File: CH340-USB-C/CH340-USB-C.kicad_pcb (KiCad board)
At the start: 2 copper layers, 18 parts, among them J1 USB_C_Receptacle_USB2.0, J2 Conn_01x05_Female, SW1 SW_Push_SPDT, U1 XC6206PxxxMR, U2 CH340N

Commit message: 初步排好電路板
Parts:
- moved J2 51.9 mm to (144.3, 105.6), turned to 180 degrees
- moved F1 42.4 mm to (74.2, 104.4), turned to -90 degrees
- moved J1 35.2 mm to (67.5, 96.5), turned to -90 degrees
- moved C1 35.2 mm to (76.5, 104.4), turned to -90 degrees
- moved C3 29.6 mm to (82.5, 99.5), turned to 90 degrees
- moved C4 25.6 mm to (82.5, 96.0), turned to -90 degrees
- moved U2 24.0 mm to (77.6, 98.0)
- moved SW1 19.8 mm to (77.8, 88.9), turned to 180 degrees
- moved C2 16.4 mm to (82.0, 104.4), turned to 90 degrees
- moved U1 14.2 mm to (79.3, 104.5), turned to 90 degrees

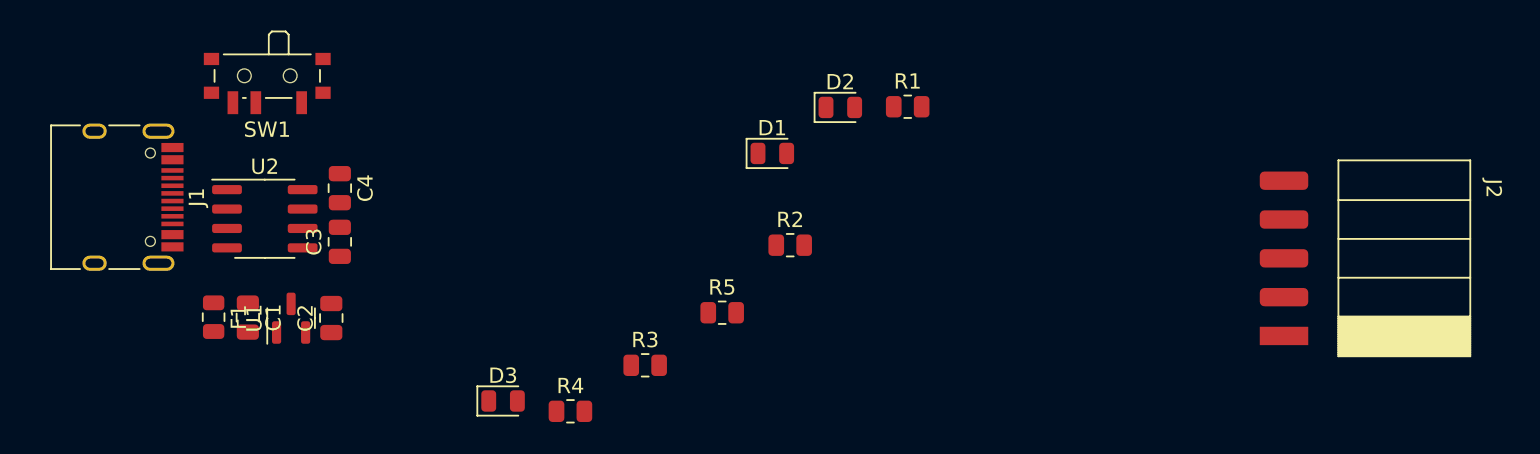
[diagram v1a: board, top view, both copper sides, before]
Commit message: 放置零件及佈線
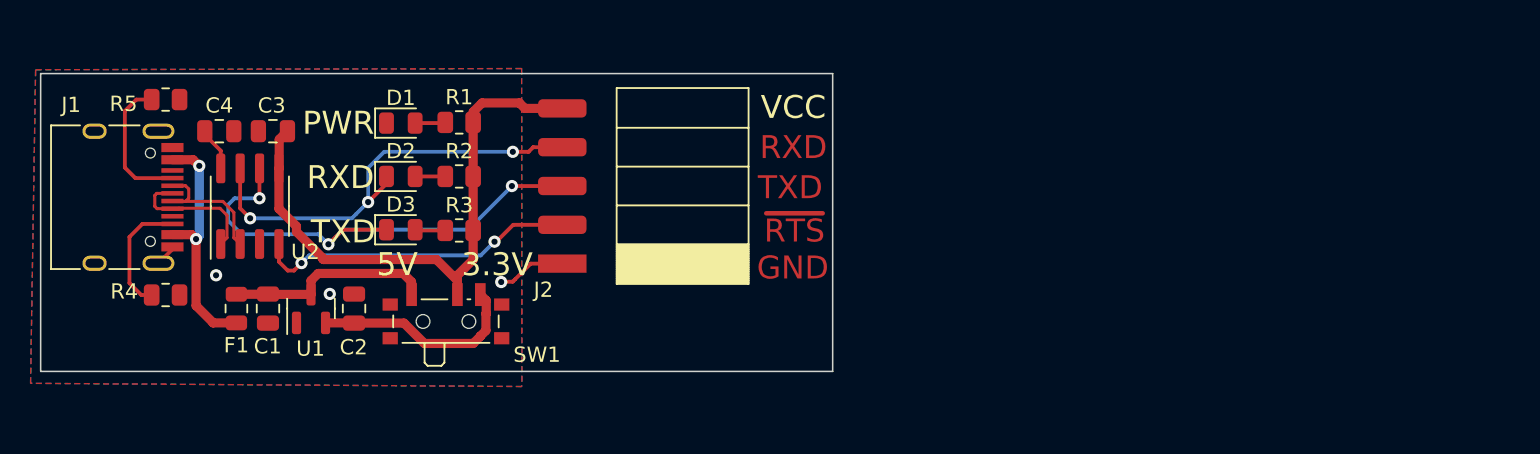
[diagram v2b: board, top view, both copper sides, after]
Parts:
- moved J2 47.5 mm to (97.1, 100.9)
- moved R5 39.0 mm to (71.1, 90.2), turned to 180 degrees
- moved R1 29.4 mm to (90.3, 91.6)
- moved D2 29.1 mm to (86.5, 95.2)
- moved R4 27.6 mm to (71.1, 102.9), turned to 180 degrees
- moved D1 24.4 mm to (86.5, 91.7)
- moved R2 22.1 mm to (90.3, 95.2)
- moved SW1 19.4 mm to (89.5, 104.3), turned to 0 degrees
- moved R3 15.0 mm to (90.3, 98.7)
- moved D3 13.1 mm to (86.5, 98.7)
- moved C4 8.73 mm to (74.6, 92.2), turned to 0 degrees
- moved C3 8.46 mm to (78.1, 92.2), turned to 180 degrees
- moved C2 1.61 mm to (83.4, 103.8)
- moved F1 1.59 mm to (75.7, 103.8), turned to 90 degrees
- moved U1 1.45 mm to (80.6, 103.8)
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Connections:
- R1 pad 2: +5V -> VCC
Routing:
- net VCC: track 0.00 -> 37.8 mm
- net /TXD: track 0.00 -> 33.5 mm, vias 0 -> 3
- net /RXD: track 0.00 -> 29.4 mm, vias 0 -> 3
- net /~{RTS}: track 0.00 -> 21.2 mm, vias 0 -> 2
- net Net-(F1-Pad1): track 0.00 -> 15.9 mm, vias 0 -> 2
- net +3V3: track 0.00 -> 13.9 mm
- net +5V: track 0.00 -> 13.6 mm
- net /CC1: track 0.00 -> 9.17 mm
- net /USBD+: track 0.00 -> 8.97 mm
- net /USBD-: track 0.00 -> 8.62 mm
- net /CC2: track 0.00 -> 7.97 mm
- net GND: track 0.00 -> 5.94 mm, vias 0 -> 3
- net /3V3: track 0.00 -> 2.87 mm
- net Net-(D3-Pad2): track 0.00 -> 1.99 mm
- net Net-(D1-Pad2): track 0.00 -> 1.99 mm
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- added copper zone on B.Cu, net GND
- added copper zone on F.Cu, net GND
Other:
- board outline added: 51.8 x 19.5 mm
- board text added: "3.3V"
- board text added: "5V"
- board text added: "GND"
- board text added: "PWR"
- board text added: "RXD"
- board text added: "TXD"
- board text added: "VCC"
- board text added: "~{RTS}"

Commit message: 調整布局
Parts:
- J2: moved to B.Cu
- moved J2 18.0 mm to (82.3, 90.6)
- moved R5 14.8 mm to (71.1, 104.9)
- moved R3 3.60 mm to (90.3, 95.1)
- moved D3 3.54 mm to (86.5, 95.1)
- moved D2 3.40 mm to (86.5, 98.6)
- moved R2 3.40 mm to (90.3, 98.6)
- moved SW1 2.31 mm to (91.8, 104.4)
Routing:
- net /TXD: track 33.5 -> 12.4 mm, vias 3 -> 2
- net /RXD: track 29.4 -> 13.9 mm, vias 3 -> 2
- net +3V3: track 13.9 -> 23.6 mm, vias 0 -> 2
- net GND: track 5.94 -> 1.45 mm, vias 3 -> 12
- net /CC1: track 9.17 -> 13.2 mm
- net +5V: track 13.6 -> 16.3 mm
- net /~{RTS}: track 21.2 -> 18.7 mm, vias 2 -> 1
- net VCC: track 37.8 -> 38.5 mm, vias 0 -> 1
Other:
- board size 51.8 x 19.5 mm -> 37.2 x 19.5 mm

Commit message: 調整布局
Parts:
- added TP1: TestPoint, TestPoint:TestPoint_Pad_D2.0mm, F.Cu at (97.9, 94.6)
- added TP2: TestPoint, TestPoint:TestPoint_Pad_D2.0mm, F.Cu at (97.9, 98.4)
- added TP3: TestPoint, TestPoint:TestPoint_Pad_D2.0mm, F.Cu at (94.2, 90.8)
- added TP4: TestPoint, TestPoint:TestPoint_Pad_D2.0mm, F.Cu at (97.9, 90.8)
- added TP5: TestPoint, TestPoint:TestPoint_Pad_D2.0mm, F.Cu at (94.1, 98.4)
- added TP6: TestPoint, TestPoint:TestPoint_Pad_D2.0mm, F.Cu at (94.2, 94.7)
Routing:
- net +5V: track 16.3 -> 35.3 mm
- net /RXD: track 13.9 -> 25.7 mm, vias 2 -> 3
- net /TXD: track 12.4 -> 24.0 mm, vias 2 -> 3
- net +3V3: track 23.6 -> 31.9 mm
- net VCC: track 38.5 -> 41.5 mm
- net GND: vias 12 -> 9

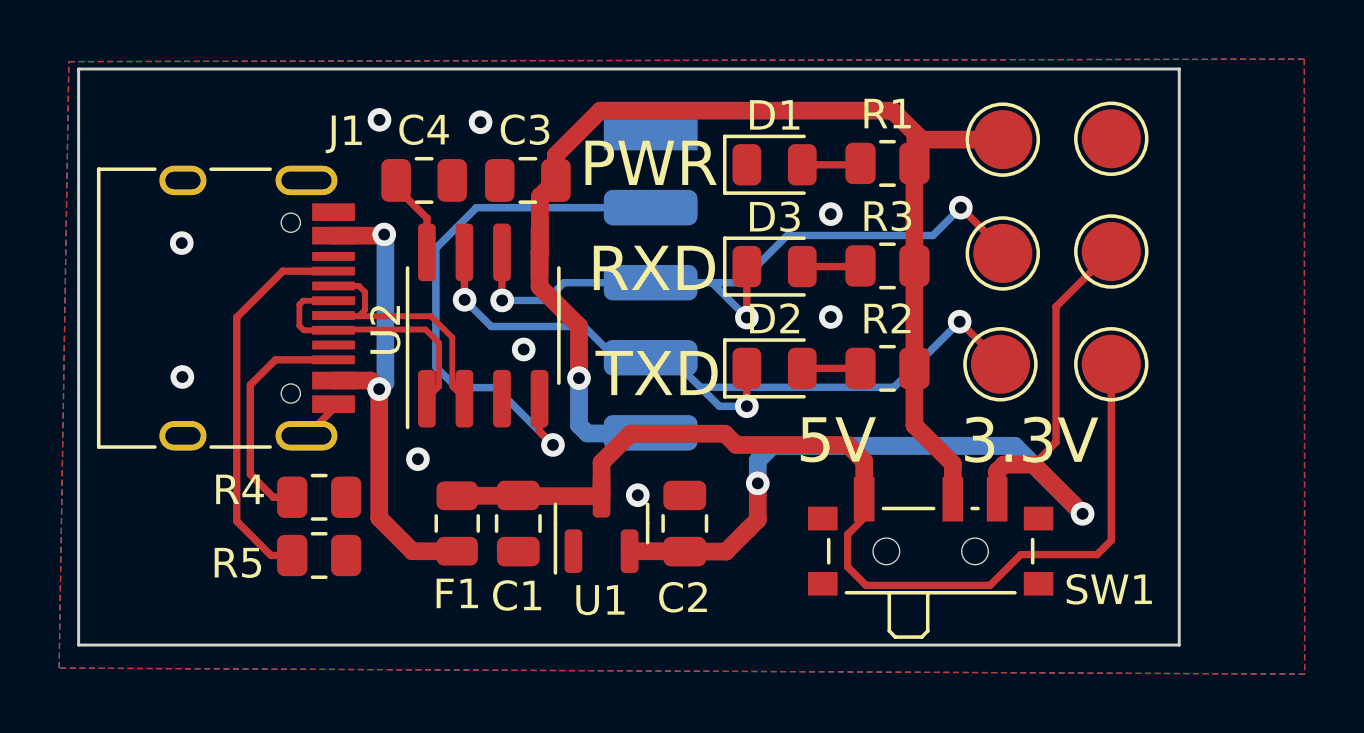
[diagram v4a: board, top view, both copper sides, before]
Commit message: 重新鋪銅
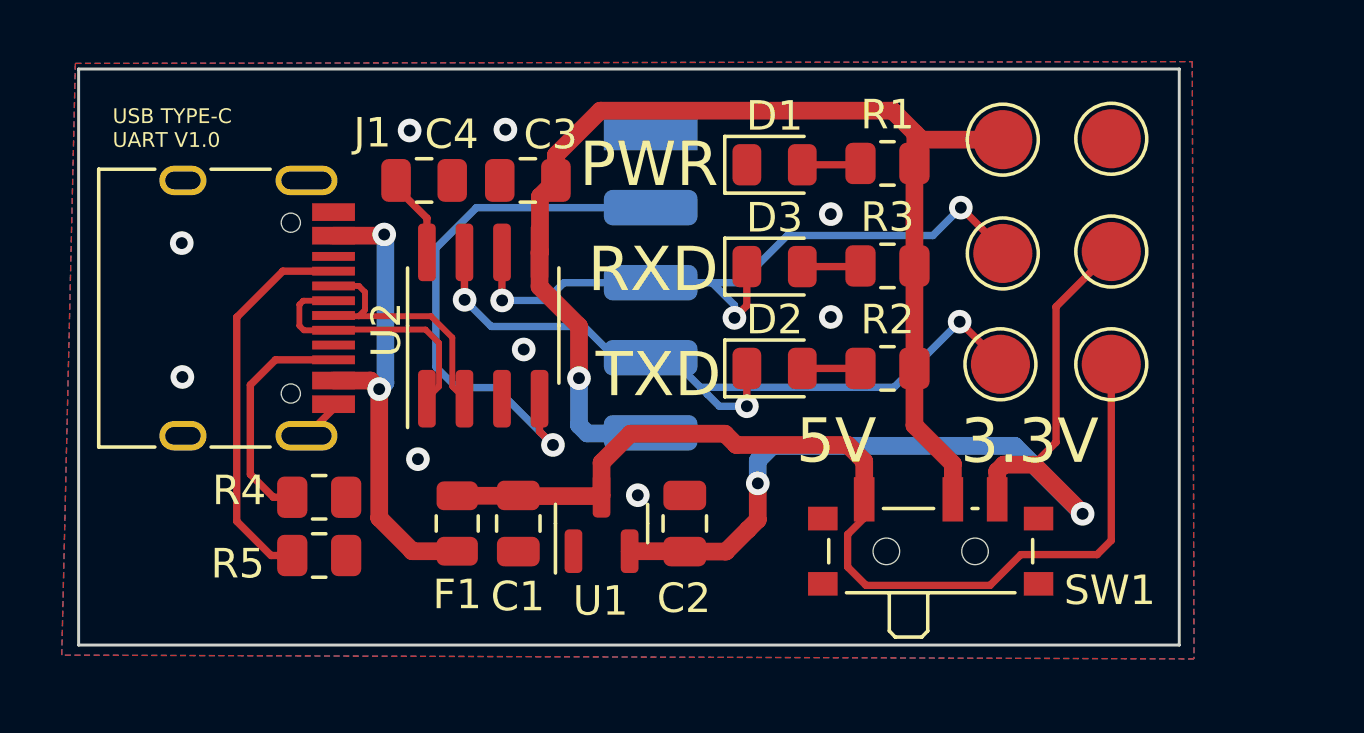
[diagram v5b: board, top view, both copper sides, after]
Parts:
- added REF**: KiCad-Logo2_5mm_SilkScreen, Symbol:KiCad-Logo2_5mm_SilkScreen, B.Cu at (72.1, 104.2)
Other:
- board text added: "USB TYPE-C UART V1.0"

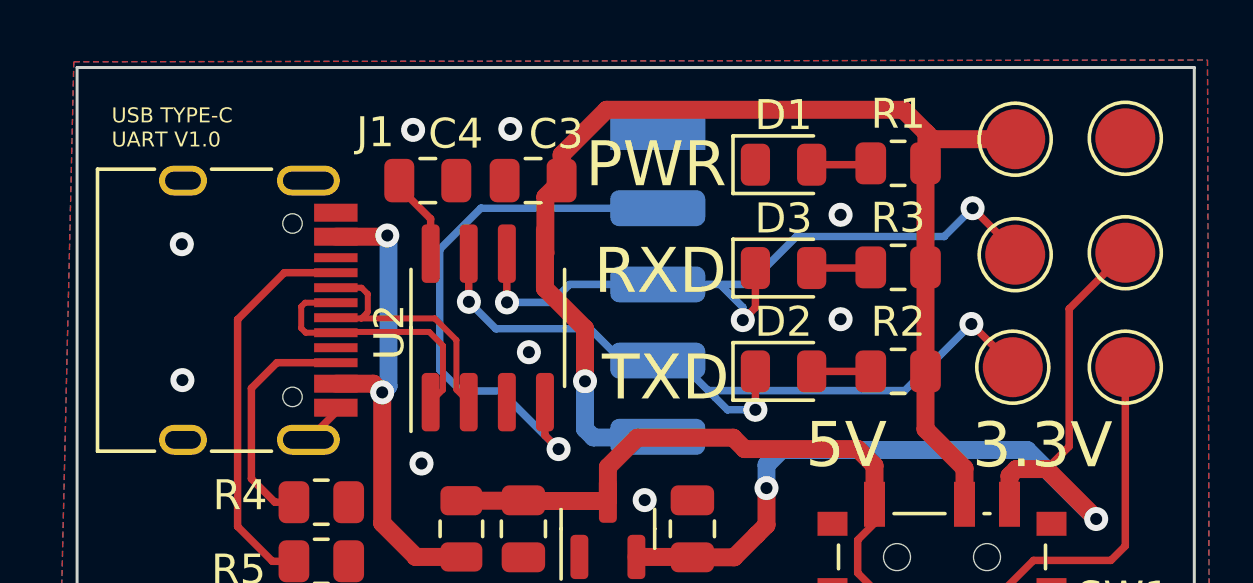
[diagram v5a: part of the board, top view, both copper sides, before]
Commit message: Update CH340-USB-C.kicad_pcb
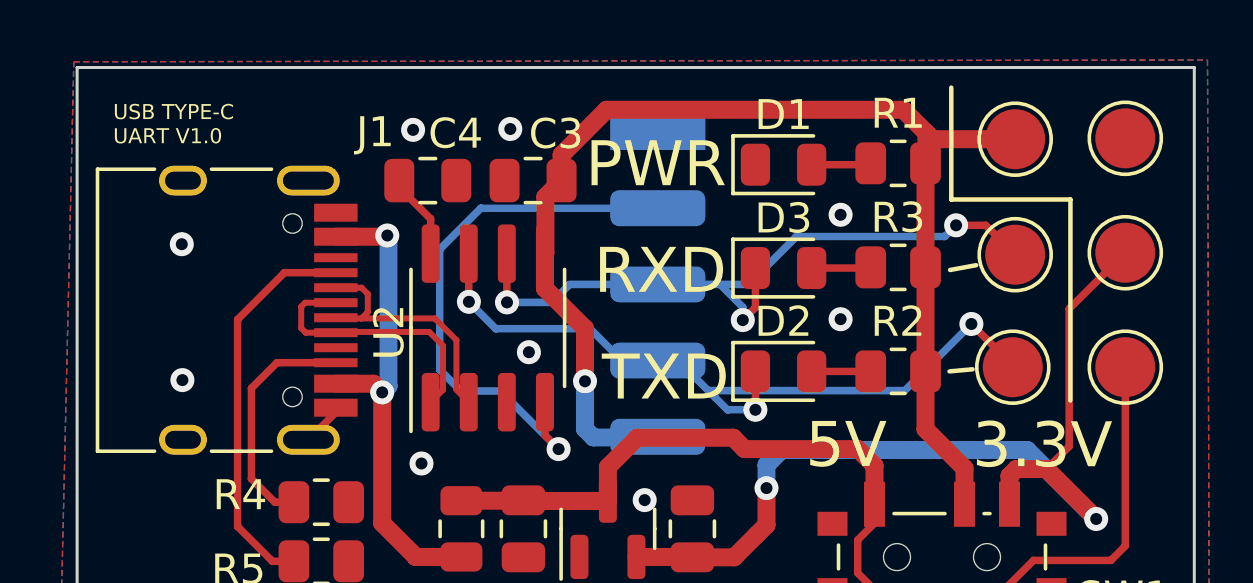
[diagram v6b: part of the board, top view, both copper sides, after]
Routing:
- net /TXD: track 24.0 -> 23.5 mm
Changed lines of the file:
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@@
     )
   )
+  (gr_line (start 92.78 98.51) (end 92.01 98.58) (layer "F.SilkS") (width 0.15))
+  (gr_line (start 92.07 89.12) (end 92.07 92.85) (layer "F.SilkS") (width 0.15))
+  (gr_line (start 96.04 92.85) (end 96.04 99.55) (layer "F.SilkS") (width 0.15))
+  (gr_line (start 92.9 95.04) (end 92.03 95.2) (layer "F.SilkS") (width 0.15))
+  (gr_line (start 92.07 92.85) (end 96.04 92.85) (layer "F.SilkS") (width 0.15))
   (gr_rect (start 62.93 88.45) (end 100.17 107.94) (layer "Edge.Cuts") (width 0.1) (fill none))
   (gr_text "~{RTS}" (at 97.377142 93.4075) (layer "B.SilkS")
@@
     (effects (font (size 1.5 1.5) (thickness 0.3)) (justify mirror))
   )
-  (gr_text "USB TYPE-C\nUART V1.0" (at 64.08 90.45) (layer "F.SilkS")
+  (gr_text "USB TYPE-C\nUART V1.0" (at 64.13 90.34) (layer "F.SilkS")
     (effects (font (size 0.5 0.5) (thickness 0.1)) (justify left))
   )
@@
   (segment (start 87.415 98.58) (end 89.385 98.58) (width 0.25) (layer "F.Cu") (net 8))
   (segment (start 85.54 96.45) (end 85.54 95.135) (width 0.25) (layer "F.Cu") (net 9))
+  (segment (start 93.22 93.71) (end 94.2 94.69) (width 0.25) (layer "F.Cu") (net 9))
+  (segment (start 92.23 93.71) (end 93.22 93.71) (width 0.25) (layer "F.Cu") (net 9))
   (segment (start 77.255 94.655) (end 77.255 96.275) (width 0.25) (layer "F.Cu") (net 9))
   (segment (start 85.12 96.87) (end 85.54 96.45) (width 0.25) (layer "F.Cu") (net 9))
-  (segment (start 94.2 94.56) (end 92.78 93.14) (width 0.25) (layer "F.Cu") (net 9))
   (segment (start 77.255 96.275) (end 77.26 96.28) (width 0.25) (layer "F.Cu") (net 9))
-  (segment (start 94.2 94.69) (end 94.2 94.56) (width 0.25) (layer "F.Cu") (net 9))
   (via (at 85.12 96.87) (size 0.8) (drill 0.4) (layers "F.Cu" "B.Cu") (net 9))
   (via (at 77.26 96.28) (size 0.8) (drill 0.4) (layers "F.Cu" "B.Cu") (net 9))
-  (via (at 92.78 93.14) (size 0.8) (drill 0.4) (layers "F.Cu" "B.Cu") (net 9))
+  (via (at 92.23 93.71) (size 0.8) (drill 0.4) (layers "F.Cu" "B.Cu") (net 9))
+  (segment (start 91.855489 94.084511) (end 86.905489 94.084511) (width 0.25) (layer "B.Cu") (net 9))
+  (segment (start 86.905489 94.084511) (end 85.31 95.68) (width 0.25) (layer "B.Cu") (net 9))
   (segment (start 85.12 96.44) (end 85.12 96.87) (width 0.25) (layer "B.Cu") (net 9))
-  (segment (start 91.835489 94.084511) (end 86.905489 94.084511) (width 0.25) (layer "B.Cu") (net 9))
   (segment (start 77.26 96.28) (end 78.75 96.28) (width 0.25) (layer "B.Cu") (net 9))
   (segment (start 78.75 96.28) (end 79.35 95.68) (width 0.25) (layer "B.Cu") (net 9))
-  (segment (start 86.905489 94.084511) (end 85.31 95.68) (width 0.25) (layer "B.Cu") (net 9))
   (segment (start 79.35 95.68) (end 82.286 95.68) (width 0.25) (layer "B.Cu") (net 9))
   (segment (start 82.286 95.68) (end 84.36 95.68) (width 0.25) (layer "B.Cu") (net 9))
   (segment (start 84.36 95.68) (end 85.12 96.44) (width 0.25) (layer "B.Cu") (net 9))
-  (segment (start 92.78 93.14) (end 91.835489 94.084511) (width 0.25) (layer "B.Cu") (net 9))
+  (segment (start 92.23 93.71) (end 91.855489 94.084511) (width 0.25) (layer "B.Cu") (net 9))
   (segment (start 85.31 95.68) (end 84.36 95.68) (width 0.25) (layer "B.Cu") (net 9))
   (segment (start 89.3625 95.135) (end 89.385 95.1125) (width 0.25) (layer "F.Cu") (net 10))
